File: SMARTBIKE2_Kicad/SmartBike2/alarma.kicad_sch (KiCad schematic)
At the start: 14 parts, among them Q6 SI2302, Q7 FDN340P, Q8 SI2302, U2 NA555D

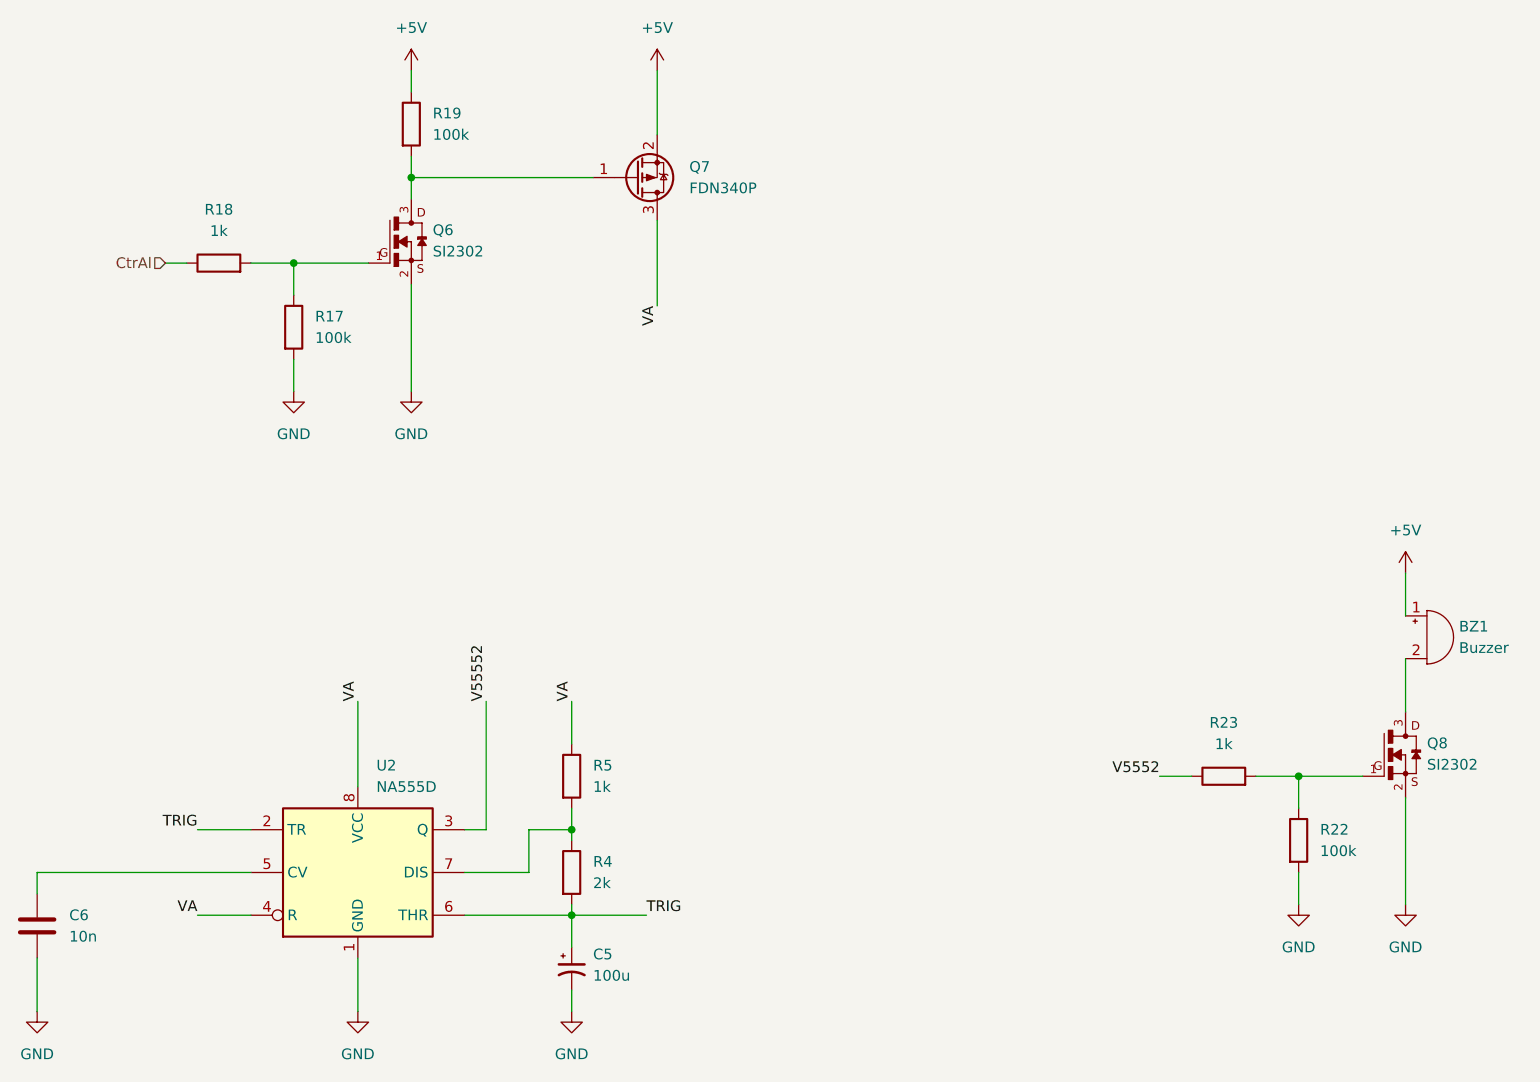
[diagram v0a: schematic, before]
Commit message: Beta 100% esquemáticos
+ Acondicionamiento ESP32

~ Huellas
~ PCB
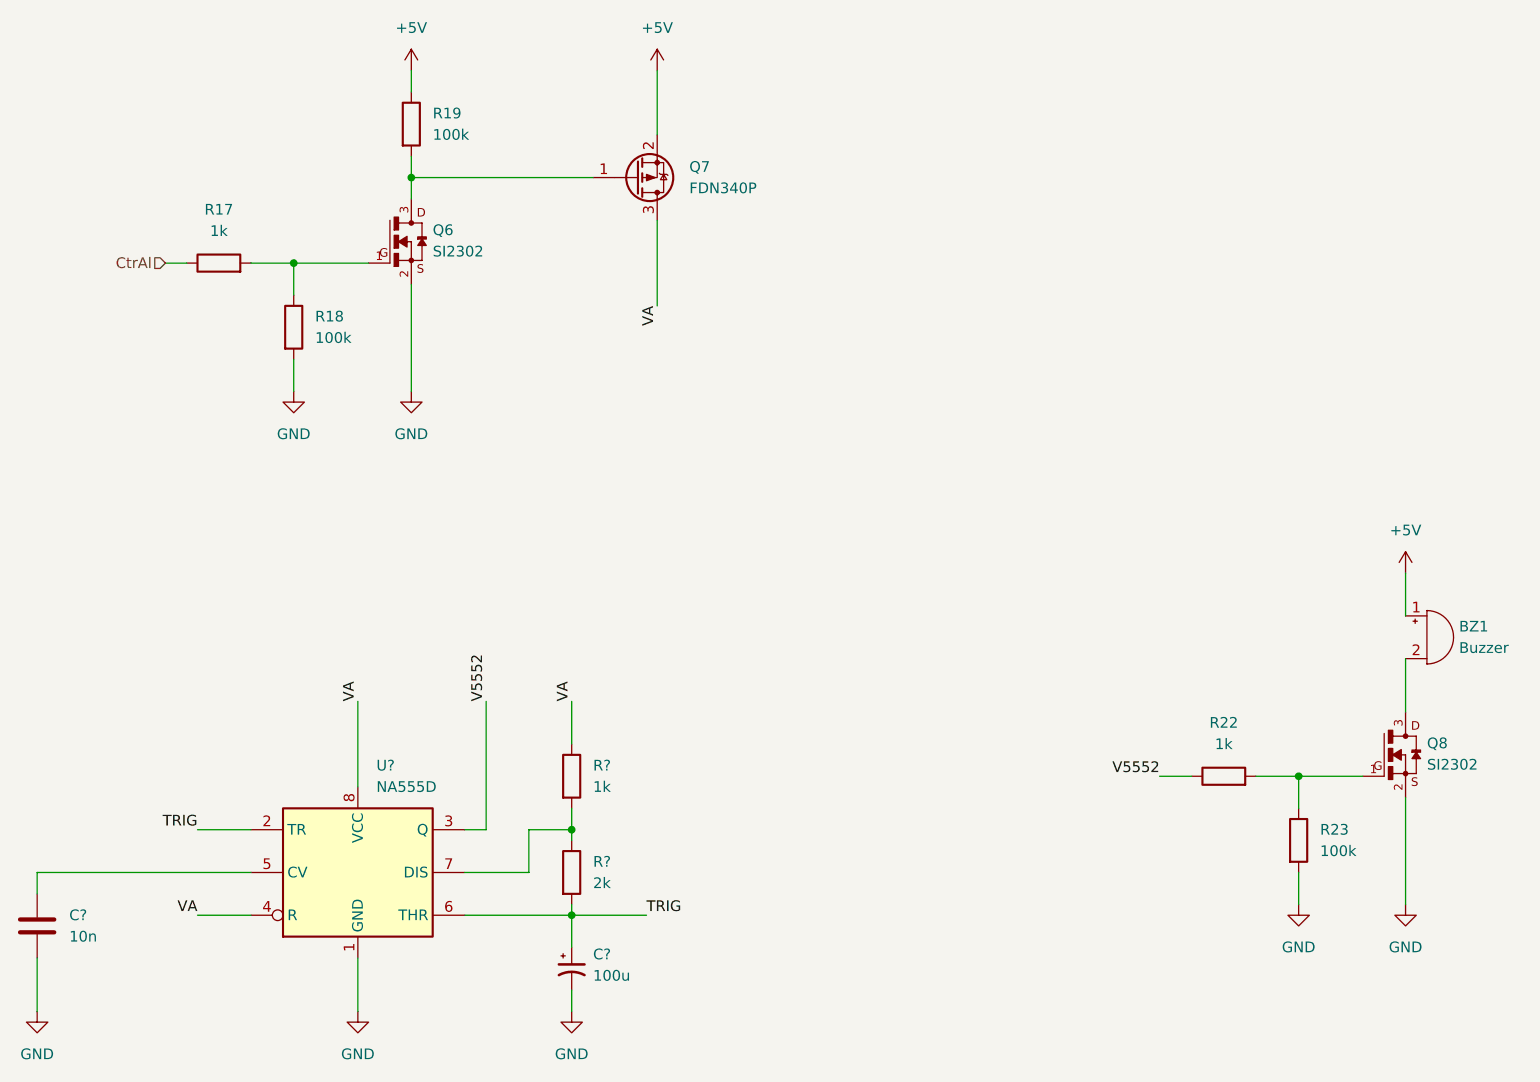
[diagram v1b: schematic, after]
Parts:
- renumbered C5 to C?, C6 to C?, R18 to R17, R17 to R18, R23 to R22, R22 to R23, R4 to R?, R5 to R?, U2 to U?
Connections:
- net V55552 is gone; now on net V5552: U?.3 (Q)

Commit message: cache
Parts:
- BZ1: footprint (none) -> Buzzer_Beeper:Buzzer_12x9.5RM7.6
- C?: footprint (none) -> Capacitor_SMD:CP_Elec_6.3x5.4
- C?: footprint (none) -> Capacitor_SMD:C_0805_2012Metric_Pad1.18x1.45mm_HandSolder
- Q6, Q8: footprint SI2302:SOT23 -> Package_TO_SOT_SMD:SOT-23
- Q7: footprint Package_TO_SOT_SMD:SOT-23 -> Package_TO_SOT_SMD:SuperSOT-3
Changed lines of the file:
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@@
       (effects (font (size 1.27 1.27)) (justify left))
     )
-    (property "Footprint" "" (at 106.68 137.16 0)
+    (property "Footprint" "Capacitor_SMD:CP_Elec_6.3x5.4" (at 106.68 137.16 0)
       (effects (font (size 1.27 1.27)) hide)
     )
@@
       (effects (font (size 1.27 1.27)) (justify left))
     )
-    (property "Footprint" "Package_TO_SOT_SMD:SOT-23" (at 119.38 41.275 0)
+    (property "Footprint" "Package_TO_SOT_SMD:SuperSOT-3" (at 119.38 41.275 0)
       (effects (font (size 1.27 1.27) italic) (justify left) hide)
     )
@@
       (effects (font (size 1.27 1.27)) (justify left))
     )
-    (property "Footprint" "SI2302:SOT23" (at 205.74 111.76 0)
+    (property "Footprint" "Package_TO_SOT_SMD:SOT-23" (at 205.74 111.76 0)
       (effects (font (size 1.27 1.27)) (justify bottom) hide)
     )
@@
       (effects (font (size 1.27 1.27)) (justify left))
     )
-    (property "Footprint" "" (at 44.1452 135.89 0)
+    (property "Footprint" "Capacitor_SMD:C_0805_2012Metric_Pad1.18x1.45mm_HandSolder" (at 44.1452 135.89 0)
       (effects (font (size 1.27 1.27)) hide)
     )
@@
       (effects (font (size 1.27 1.27)) (justify left))
     )
-    (property "Footprint" "SI2302:SOT23" (at 87.63 50.8 0)
+    (property "Footprint" "Package_TO_SOT_SMD:SOT-23" (at 87.63 50.8 0)
       (effects (font (size 1.27 1.27)) (justify bottom) hide)
     )
@@
       (effects (font (size 1.27 1.27)) (justify left))
     )
-    (property "Footprint" "" (at 207.645 95.25 90)
-      (effects (font (size 1.27 1.27)) hide)
-    )
+    (property "Footprint" "Buzzer_Beeper:Buzzer_12x9.5RM7.6" (at 207.645 95.25 90)
+      (effects (font (size 1.27 1.27)) hide)
+    )

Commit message: Mas huellas
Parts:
- R17, R18, R19, R22, R23, R? (x2): footprint (none) -> Resistor_SMD:R_0805_2012Metric_Pad1.20x1.40mm_HandSolder
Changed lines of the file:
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@@
       (effects (font (size 1.27 1.27)) (justify left))
     )
-    (property "Footprint" "" (at 191.262 121.92 90)
+    (property "Footprint" "Resistor_SMD:R_0805_2012Metric_Pad1.20x1.40mm_HandSolder" (at 191.262 121.92 90)
       (effects (font (size 1.27 1.27)) hide)
     )
@@
       (effects (font (size 1.27 1.27)) (justify left))
     )
-    (property "Footprint" "" (at 104.902 125.73 90)
+    (property "Footprint" "Resistor_SMD:R_0805_2012Metric_Pad1.20x1.40mm_HandSolder" (at 104.902 125.73 90)
       (effects (font (size 1.27 1.27)) hide)
     )
@@
       (effects (font (size 1.27 1.27)) (justify left))
     )
-    (property "Footprint" "" (at 104.902 114.3 90)
+    (property "Footprint" "Resistor_SMD:R_0805_2012Metric_Pad1.20x1.40mm_HandSolder" (at 104.902 114.3 90)
       (effects (font (size 1.27 1.27)) hide)
     )
@@
       (effects (font (size 1.27 1.27)))
     )
-    (property "Footprint" "" (at 64.77 55.118 90)
+    (property "Footprint" "Resistor_SMD:R_0805_2012Metric_Pad1.20x1.40mm_HandSolder" (at 64.77 55.118 90)
       (effects (font (size 1.27 1.27)) hide)
     )
@@
       (effects (font (size 1.27 1.27)) (justify left))
     )
-    (property "Footprint" "" (at 85.852 36.83 90)
+    (property "Footprint" "Resistor_SMD:R_0805_2012Metric_Pad1.20x1.40mm_HandSolder" (at 85.852 36.83 90)
       (effects (font (size 1.27 1.27)) hide)
     )
@@
       (effects (font (size 1.27 1.27)))
     )
-    (property "Footprint" "" (at 184.15 116.078 90)
+    (property "Footprint" "Resistor_SMD:R_0805_2012Metric_Pad1.20x1.40mm_HandSolder" (at 184.15 116.078 90)
       (effects (font (size 1.27 1.27)) hide)
     )
@@
       (effects (font (size 1.27 1.27)) (justify left))
     )
-    (property "Footprint" "" (at 71.882 60.96 90)
-      (effects (font (size 1.27 1.27)) hide)
-    )
+    (property "Footprint" "Resistor_SMD:R_0805_2012Metric_Pad1.20x1.40mm_HandSolder" (at 71.882 60.96 90)
+      (effects (font (size 1.27 1.27)) hide)
+    )

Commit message: diseño PCB1.0
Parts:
- BZ1: footprint Buzzer_Beeper:Buzzer_12x9.5RM7.6 -> Connector_PinHeader_2.54mm:PinHeader_1x02_P2.54mm_Vertical
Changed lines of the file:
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@@
       (effects (font (size 1.27 1.27)) (justify left))
     )
-    (property "Footprint" "Buzzer_Beeper:Buzzer_12x9.5RM7.6" (at 207.645 95.25 90)
+    (property "Footprint" "Connector_PinHeader_2.54mm:PinHeader_1x02_P2.54mm_Vertical" (at 207.645 95.25 90)
       (effects (font (size 1.27 1.27)) hide)
     )
